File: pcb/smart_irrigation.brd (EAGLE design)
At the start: 76.2 x 76.2 mm, 31 parts, among them IC1 TMP36, IC2 7805DT, IC3 7833DT, IC4 DS1307, J1 1X2-3.5MM, Q1 IRF730, Q2 32.768, Q3 2N3904, U1 BL600

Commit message: PCB: Give names to all signals.
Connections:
- net FLOW_OUT renamed FLOW_DATA
- net N$12 renamed SIO_4
- net N$13 renamed SIO_5
- net N$14 renamed SIO_6
- net N$16 renamed SIO_20
- net N$2 renamed SIO_7
- net N$20 renamed NRESET
- net N$21 renamed SIO_16
- net N$22 renamed SIO_15
- net N$23 renamed SIO_14
- net N$24 renamed SIO_13
- net N$25 renamed SIO_12/SCK
- net N$26 renamed SIO_11/MISO
- net N$27 renamed SIO_10/MOSI
- net N$4 renamed SIO_25
- net N$5 renamed SIO_26
- net N$6 renamed SIO_27
- net N$7 renamed SIO_29
- net RAIN_OUT renamed RAIN_DATA
- net RTC_OUT renamed RTC_DATA
- net SOIL_OUT renamed SOIL_DATA
- net TEMP_OUT renamed TEMP_DATA
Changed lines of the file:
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@@
 <wire x1="32.852" y1="27.178" x2="32.75" y2="27.28" width="0.254" layer="16"/>
 </signal>
-<signal name="N$2">
+<signal name="SIO_7">
 <contactref element="U1" pad="J5_5"/>
 <contactref element="JP4" pad="5"/>
@@
 <wire x1="32.806" y1="21.336" x2="32.75" y2="21.28" width="0.254" layer="16"/>
 </signal>
-<signal name="N$4">
+<signal name="SIO_25">
 <contactref element="JP3" pad="2"/>
 <contactref element="U1" pad="36"/>
@@
 <wire x1="27.362" y1="44.52" x2="26.162" y2="45.72" width="0.254" layer="16"/>
 </signal>
-<signal name="N$5">
+<signal name="SIO_26">
 <contactref element="U1" pad="38"/>
 <contactref element="JP3" pad="3"/>
@@
 <wire x1="26.232" y1="43.25" x2="26.162" y2="43.18" width="0.254" layer="16"/>
 </signal>
-<signal name="N$6">
+<signal name="SIO_27">
 <contactref element="JP3" pad="4"/>
 <contactref element="U1" pad="39"/>
@@
 <wire x1="27.502" y1="41.98" x2="26.162" y2="40.64" width="0.254" layer="16"/>
 </signal>
-<signal name="N$7">
+<signal name="SIO_29">
 <contactref element="U1" pad="41"/>
 <contactref element="JP3" pad="5"/>
@@
 <wire x1="24.638" y1="35.56" x2="26.162" y2="35.56" width="0.254" layer="16"/>
 </signal>
-<signal name="TEMP_OUT">
+<signal name="TEMP_DATA">
 <contactref element="JP3" pad="7"/>
 <contactref element="U1" pad="2"/>
@@
 <wire x1="23.876" y1="33.02" x2="26.162" y2="33.02" width="0.254" layer="16"/>
 </signal>
-<signal name="SOIL_OUT">
+<signal name="SOIL_DATA">
 <contactref element="U1" pad="4"/>
 <contactref element="JP3" pad="8"/>
@@
 <wire x1="6.096" y1="30.48" x2="26.162" y2="30.48" width="0.254" layer="1"/>
 </signal>
-<signal name="RAIN_OUT">
+<signal name="RAIN_DATA">
 <contactref element="JP3" pad="9"/>
 <contactref element="U1" pad="5"/>
@@
 <wire x1="27.208" y1="11.684" x2="27.24" y2="11.652" width="0.254" layer="16"/>
 </signal>
-<signal name="N$12">
+<signal name="SIO_4">
 <contactref element="U1" pad="6"/>
 <contactref element="JP3" pad="10"/>
@@
 <wire x1="27.686" y1="25.4" x2="26.162" y2="25.4" width="0.254" layer="16"/>
 </signal>
-<signal name="N$13">
+<signal name="SIO_5">
 <contactref element="JP3" pad="11"/>
 <contactref element="U1" pad="7"/>
@@
 <wire x1="27.432" y1="22.86" x2="26.162" y2="22.86" width="0.254" layer="16"/>
 </signal>
-<signal name="N$14">
+<signal name="SIO_6">
 <contactref element="U1" pad="8"/>
 <contactref element="JP3" pad="12"/>
@@
 <wire x1="27.178" y1="20.32" x2="26.162" y2="20.32" width="0.254" layer="16"/>
 </signal>
-<signal name="N$16">
+<signal name="SIO_20">
 <contactref element="JP6" pad="2"/>
 <contactref element="U1" pad="27"/>
@@
 <wire x1="57.912" y1="50.546" x2="59.182" y2="50.546" width="0.254" layer="16"/>
 </signal>
-<signal name="RTC_OUT">
+<signal name="RTC_DATA">
 <contactref element="U1" pad="26"/>
 <contactref element="JP6" pad="3"/>
@@
 <wire x1="60.96" y1="48.006" x2="59.182" y2="48.006" width="0.254" layer="16"/>
 </signal>
-<signal name="FLOW_OUT">
+<signal name="FLOW_DATA">
 <contactref element="JP6" pad="4"/>
 <contactref element="U1" pad="25"/>
@@
 <wire x1="59.182" y1="42.926" x2="67.564" y2="42.926" width="0.254" layer="16"/>
 </signal>
-<signal name="N$20">
+<signal name="NRESET">
 <contactref element="JP6" pad="6"/>
 <contactref element="U1" pad="22"/>
@@
 <wire x1="58.276" y1="39.48" x2="59.182" y2="40.386" width="0.254" layer="16"/>
 </signal>
-<signal name="N$21">
+<signal name="SIO_16">
 <contactref element="U1" pad="21"/>
 <contactref element="JP6" pad="7"/>
@@
 <wire x1="58.818" y1="38.21" x2="59.182" y2="37.846" width="0.254" layer="16"/>
 </signal>
-<signal name="N$22">
+<signal name="SIO_15">
 <contactref element="JP6" pad="8"/>
 <contactref element="U1" pad="20"/>
@@
 <wire x1="57.658" y1="35.306" x2="59.182" y2="35.306" width="0.254" layer="16"/>
 </signal>
-<signal name="N$23">
+<signal name="SIO_14">
 <contactref element="U1" pad="19"/>
 <contactref element="JP6" pad="9"/>
@@
 <wire x1="57.658" y1="32.766" x2="59.182" y2="32.766" width="0.254" layer="16"/>
 </signal>
-<signal name="N$24">
+<signal name="SIO_13">
 <contactref element="JP6" pad="10"/>
 <contactref element="U1" pad="18"/>
@@
 <wire x1="58.166" y1="30.226" x2="59.182" y2="30.226" width="0.254" layer="16"/>
 </signal>
-<signal name="N$25">
+<signal name="SIO_12/SCK">
 <contactref element="U1" pad="16"/>
 <contactref element="JP6" pad="11"/>
@@
 <wire x1="53.738" y1="33.13" x2="59.182" y2="27.686" width="0.254" layer="16"/>
 </signal>
-<signal name="N$26">
+<signal name="SIO_11/MISO">
 <contactref element="JP6" pad="12"/>
 <contactref element="U1" pad="15"/>
@@
 <wire x1="57.912" y1="25.146" x2="59.182" y2="25.146" width="0.254" layer="16"/>
 </signal>
-<signal name="N$27">
+<signal name="SIO_10/MOSI">
 <contactref element="U1" pad="14"/>
 <contactref element="JP6" pad="13"/>

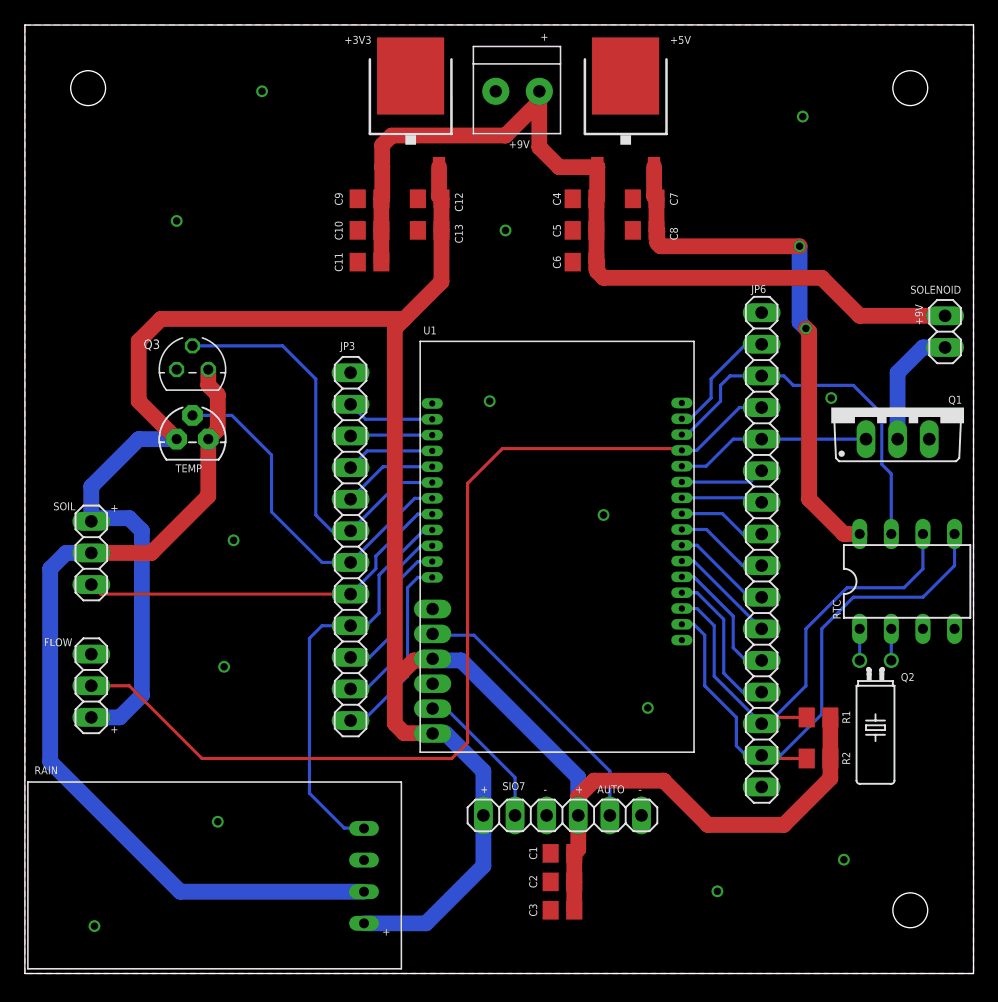
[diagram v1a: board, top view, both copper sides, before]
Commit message: PCB: Fix spacing between headers on BL600 package
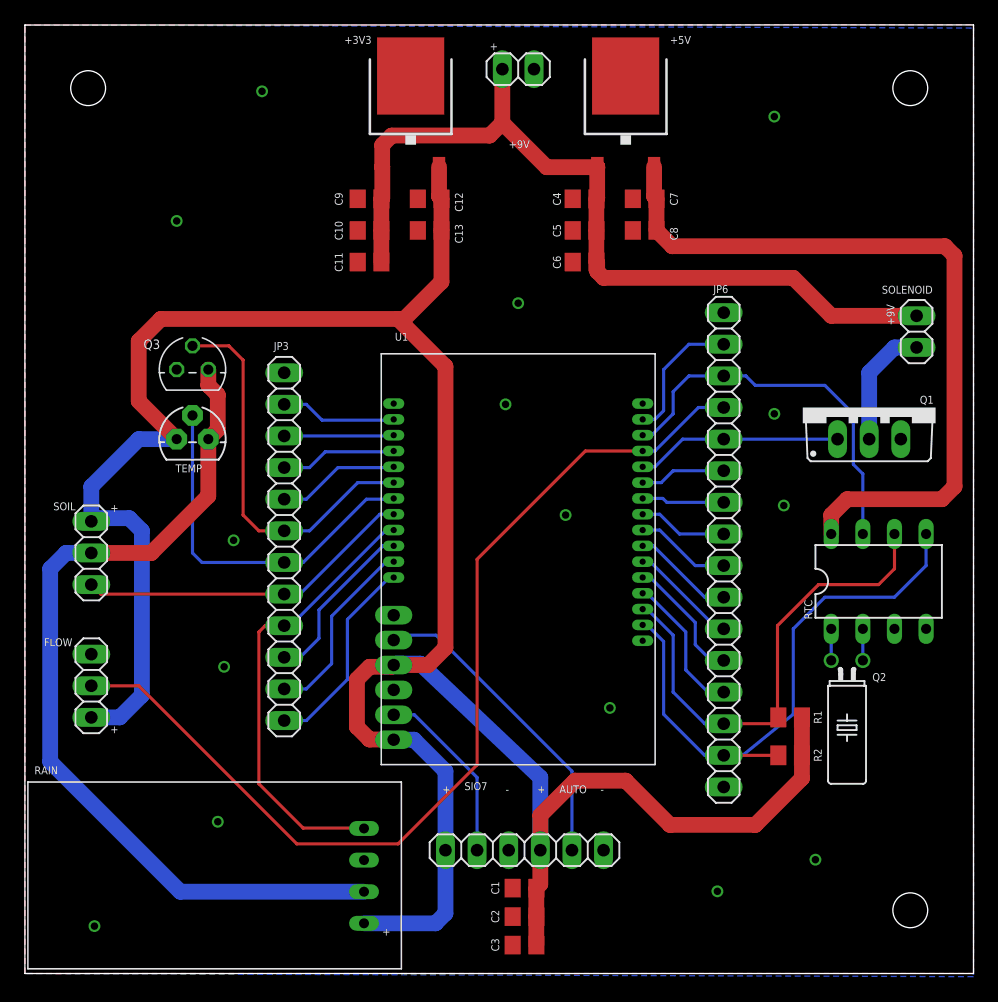
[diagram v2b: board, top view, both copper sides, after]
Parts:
- J1: value 1X2-3.5MM -> (none); device adafruit:1X2-3.5MM -> pinhead:1X02
- moved JP3 5.33 mm to (20.8, 34.3)
- moved C1 4.13 mm to (40.1, 6.86)
- moved C2 4.13 mm to (40.1, 4.57)
- moved C3 4.13 mm to (40.1, 2.29)
- moved JP4 4.13 mm to (40.1, 9.91)
- moved JP6 3.05 mm to (56.1, 34.0)
- moved U1 2.34 mm to (39.6, 33.8)
- moved R2 2.30 mm to (61.5, 17.5)
- moved IC4 2.29 mm to (68.6, 31.5)
- moved JP5 2.29 mm to (71.6, 51.6)
- moved Q1 2.29 mm to (67.8, 45.5)
- moved R1 2.29 mm to (61.5, 20.6)
- moved Q2 2.29 mm to (66.0, 25.1)
- moved J1 1.78 mm to (39.6, 72.6)
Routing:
- net +5V: track 43.6 -> 60.9 mm, vias 2 -> 0
- net +3V3: track 199.6 -> 207.4 mm
- net SOIL_DATA: track 31.0 -> 27.3 mm
- net +9V: track 72.1 -> 68.9 mm
- net RAIN_DATA: track 33.2 -> 36.3 mm
- net NAUTORUN: track 22.4 -> 25.4 mm
- net SIO_7: track 12.0 -> 14.6 mm
- net SIO_25: track 7.06 -> 9.35 mm
- net SIO_27: track 7.11 -> 9.35 mm
- net SIO_26: track 6.59 -> 8.82 mm
- net SIO_29: track 7.64 -> 9.87 mm
- net SENSORS_ENABLE: track 33.4 -> 31.2 mm
- net RTC_DATA: track 30.0 -> 31.2 mm
- net SIO_20: track 9.78 -> 10.9 mm
- net SDA: track 46.6 -> 47.6 mm
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
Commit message: PCB: Change flow sensor GPIO pin
The flow sensor's pin was on the opposite side of the other sensors,
making for awkward routing.
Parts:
- moved JP7 23.9 mm to (5.33, 47.0)
- moved IC1 0.25 mm to (13.5, 42.7)
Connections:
- removed net SIO_29: JP3.5, U1.41
- new net SIO_18: JP6.4, U1.25
- net FLOW_DATA: now also JP3.5, U1.41; no longer JP6.4, U1.25
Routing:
- net FLOW_DATA: track 80.3 -> 32.3 mm
- net +3V3: track 207.4 -> 186.4 mm
- net SIO_29: track 9.87 -> 0.00 mm
- net SIO_18: track 0.00 -> 7.96 mm
- net TEMP_DATA: track 29.7 -> 27.2 mm
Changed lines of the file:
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@@
 <text x="4.064" y="37.846" size="0.635" layer="25" font="vector" ratio="20" rot="R180">SOIL</text>
 <text x="6.858" y="37.084" size="0.635" layer="25" font="vector" ratio="20">+</text>
-<text x="3.81" y="26.924" size="0.635" layer="25" font="vector" ratio="20" rot="R180">FLOW</text>
+<text x="4.572" y="51.562" size="0.635" layer="25" font="vector" ratio="20" rot="R180">FLOW</text>
 <text x="6.858" y="19.304" size="0.635" layer="25" font="vector" ratio="20">+</text>
 <text x="0.762" y="16.002" size="0.635" layer="25" font="vector" ratio="20">RAIN</text>
@@
 <attribute name="NAME" x="64.008" y="20.066" size="0.635" layer="25" font="vector" ratio="20" rot="R90"/>
 </element>
-<element name="IC1" library="smart_irrigation" package="TO92" value="TMP36" x="13.462" y="42.926" smashed="yes"/>
+<element name="IC1" library="smart_irrigation" package="TO92" value="TMP36" x="13.462" y="42.672" smashed="yes"/>
 <element name="JP2" library="pinhead" package="1X03" value="" x="5.334" y="33.782" smashed="yes" rot="R270">
 <attribute name="VALUE" x="2.159" y="37.592" size="1.27" layer="27" rot="R270"/>
@@
 <attribute name="NAME" x="38.1" y="1.778" size="0.635" layer="25" font="vector" ratio="20" rot="R90"/>
 </element>
-<element name="JP7" library="smart_irrigation" package="1X03" value="" x="5.334" y="23.114" smashed="yes" rot="R90">
-<attribute name="VALUE" x="8.509" y="19.304" size="1.27" layer="27" rot="R90"/>
+<element name="JP7" library="smart_irrigation" package="1X03" value="" x="5.334" y="46.99" smashed="yes" rot="R90">
+<attribute name="VALUE" x="8.509" y="43.18" size="1.27" layer="27" rot="R90"/>
 </element>
 <element name="Q1" library="smart_irrigation" package="TO220" value="IRF730" x="67.818" y="45.466" smashed="yes">
@@
 <wire x1="31.75" y1="24.892" x2="29.836" y2="24.892" width="1.27" layer="16"/>
 <wire x1="29.836" y1="24.892" x2="29.624" y2="24.782" width="1.27" layer="16"/>
-<wire x1="5.334" y1="20.574" x2="7.62" y2="20.574" width="1.27" layer="16"/>
-<wire x1="7.62" y1="20.574" x2="9.398" y2="22.352" width="1.27" layer="16"/>
-<wire x1="9.398" y1="22.352" x2="9.398" y2="35.56" width="1.27" layer="16"/>
-<wire x1="9.398" y1="35.56" x2="8.382" y2="36.576" width="1.27" layer="16"/>
-<wire x1="8.382" y1="36.576" x2="5.588" y2="36.576" width="1.27" layer="16"/>
-<wire x1="5.588" y1="36.576" x2="5.334" y2="36.322" width="1.27" layer="16"/>
-<wire x1="12.192" y1="42.926" x2="9.144" y2="42.926" width="1.27" layer="16"/>
-<wire x1="9.144" y1="42.926" x2="5.334" y2="39.116" width="1.27" layer="16"/>
-<wire x1="5.334" y1="39.116" x2="5.334" y2="36.322" width="1.27" layer="16"/>
 <wire x1="33.462" y1="59.69" x2="33.462" y2="55.56" width="1.27" layer="1"/>
 <wire x1="33.462" y1="55.56" x2="30.48" y2="52.578" width="1.27" layer="1"/>
@@
 <wire x1="29.972" y1="52.578" x2="10.922" y2="52.578" width="1.27" layer="1"/>
 <wire x1="10.922" y1="52.578" x2="9.144" y2="50.8" width="1.27" layer="1"/>
-<wire x1="9.144" y1="50.8" x2="9.144" y2="45.974" width="1.27" layer="1"/>
-<wire x1="9.144" y1="45.974" x2="12.192" y2="42.926" width="1.27" layer="1"/>
+<wire x1="9.144" y1="50.8" x2="9.144" y2="45.72" width="1.27" layer="1"/>
+<wire x1="9.144" y1="45.72" x2="12.192" y2="42.672" width="1.27" layer="1"/>
 <contactref element="C3" pad="1"/>
 <wire x1="41.082" y1="4.572" x2="41.082" y2="2.286" width="1.27" layer="1"/>
@@
 <wire x1="33.782" y1="16.256" x2="31.256" y2="18.782" width="1.27" layer="16"/>
 <wire x1="31.256" y1="18.782" x2="29.624" y2="18.782" width="1.27" layer="16"/>
+<wire x1="5.334" y1="36.322" x2="5.334" y2="44.45" width="1.27" layer="1"/>
+<wire x1="5.334" y1="44.45" x2="8.128" y2="44.45" width="1.27" layer="1"/>
+<wire x1="8.128" y1="44.45" x2="9.144" y2="45.72" width="1.27" layer="1"/>
 </signal>
 <signal name="NAUTORUN">
@@
 <wire x1="29.562" y1="41.91" x2="29.624" y2="41.972" width="0.254" layer="16"/>
 </signal>
-<signal name="SIO_29">
+<signal name="FLOW_DATA">
 <contactref element="U1" pad="41"/>
 <contactref element="JP3" pad="5"/>
@@
 <wire x1="25.146" y1="40.64" x2="29.562" y2="40.64" width="0.254" layer="16"/>
 <wire x1="29.562" y1="40.64" x2="29.624" y2="40.702" width="0.254" layer="16"/>
+<contactref element="JP7" pad="2"/>
+<wire x1="5.334" y1="46.99" x2="7.874" y2="46.99" width="0.254" layer="16"/>
+<wire x1="7.874" y1="46.99" x2="8.89" y2="46.228" width="0.254" layer="16"/>
+<wire x1="8.89" y1="46.228" x2="16.764" y2="46.228" width="0.254" layer="16"/>
+<wire x1="16.764" y1="46.228" x2="18.542" y2="44.45" width="0.254" layer="16"/>
+<wire x1="18.542" y1="44.45" x2="18.542" y2="38.862" width="0.254" layer="16"/>
+<wire x1="18.542" y1="38.862" x2="19.304" y2="38.1" width="0.254" layer="16"/>
+<wire x1="19.304" y1="38.1" x2="20.828" y2="38.1" width="0.254" layer="16"/>
 </signal>
 <signal name="SENSORS_ENABLE">
@@
 <contactref element="U1" pad="2"/>
 <contactref element="IC1" pad="2"/>
-<wire x1="13.462" y1="44.831" x2="13.462" y2="33.782" width="0.254" layer="16"/>
-<wire x1="13.462" y1="33.782" x2="14.224" y2="33.02" width="0.254" layer="16"/>
-<wire x1="14.224" y1="33.02" x2="20.828" y2="33.02" width="0.254" layer="16"/>
 <wire x1="20.828" y1="33.02" x2="22.352" y2="33.02" width="0.254" layer="16"/>
 <wire x1="22.352" y1="33.02" x2="27.432" y2="38.1" width="0.254" layer="16"/>
 <wire x1="27.432" y1="38.1" x2="29.562" y2="38.1" width="0.254" layer="16"/>
 <wire x1="29.562" y1="38.1" x2="29.624" y2="38.162" width="0.254" layer="16"/>
+<wire x1="20.828" y1="33.02" x2="20.066" y2="33.02" width="0.254" layer="16"/>
+<wire x1="20.066" y1="33.02" x2="16.51" y2="36.576" width="0.254" layer="16"/>
+<wire x1="16.51" y1="36.576" x2="16.51" y2="43.434" width="0.254" layer="16"/>
+<wire x1="16.51" y1="43.434" x2="15.24" y2="44.704" width="0.254" layer="16"/>
+<wire x1="15.24" y1="44.704" x2="13.589" y2="44.704" width="0.254" layer="16"/>
+<wire x1="13.589" y1="44.704" x2="13.462" y2="44.577" width="0.254" layer="16"/>
 </signal>
 <signal name="SOIL_DATA">
@@
 <wire x1="52.07" y1="46.736" x2="53.34" y2="48.006" width="0.254" layer="16"/>
 <wire x1="53.34" y1="48.006" x2="56.134" y2="48.006" width="0.254" layer="16"/>
-</signal>
-<signal name="FLOW_DATA">
-<contactref element="JP6" pad="4"/>
-<contactref element="U1" pad="25"/>
-<contactref element="JP7" pad="2"/>
-<wire x1="49.624" y1="41.972" x2="45.02" y2="41.972" width="0.254" layer="1"/>
-<wire x1="45.02" y1="41.972" x2="36.322" y2="33.274" width="0.254" layer="1"/>
-<wire x1="36.322" y1="33.274" x2="36.322" y2="16.764" width="0.254" layer="1"/>
-<wire x1="36.322" y1="16.764" x2="29.972" y2="10.414" width="0.254" layer="1"/>
-<wire x1="29.972" y1="10.414" x2="21.844" y2="10.414" width="0.254" layer="1"/>
-<wire x1="21.844" y1="10.414" x2="9.144" y2="23.114" width="0.254" layer="1"/>
-<wire x1="9.144" y1="23.114" x2="5.334" y2="23.114" width="0.254" layer="1"/>
-<wire x1="49.624" y1="41.972" x2="50.608" y2="41.972" width="0.254" layer="16"/>
-<wire x1="50.608" y1="41.972" x2="54.102" y2="45.466" width="0.254" layer="16"/>
-<wire x1="54.102" y1="45.466" x2="56.134" y2="45.466" width="0.254" layer="16"/>
 </signal>
 <signal name="SOL_ENABLE">
@@
 <wire x1="5.334" y1="33.782" x2="10.16" y2="33.782" width="1.27" layer="1"/>
 <wire x1="10.16" y1="33.782" x2="14.732" y2="38.354" width="1.27" layer="1"/>
-<wire x1="14.732" y1="38.354" x2="14.732" y2="42.926" width="1.27" layer="1"/>
+<wire x1="14.732" y1="38.354" x2="14.732" y2="42.672" width="1.27" layer="1"/>
 <wire x1="14.732" y1="48.514" x2="14.732" y2="47.244" width="1.27" layer="1"/>
-<wire x1="14.732" y1="47.244" x2="15.494" y2="46.482" width="1.27" layer="1"/>
-<wire x1="15.494" y1="46.482" x2="15.494" y2="43.688" width="1.27" layer="1"/>
-<wire x1="15.494" y1="43.688" x2="14.732" y2="42.926" width="1.27" layer="1"/>
+<wire x1="14.732" y1="47.244" x2="15.748" y2="46.228" width="1.27" layer="1"/>
+<wire x1="15.748" y1="46.228" x2="15.748" y2="43.942" width="1.27" layer="1"/>
+<wire x1="15.748" y1="43.942" x2="14.732" y2="42.672" width="1.27" layer="1"/>
 </signal>
 <signal name="N$1">
@@
 <wire x1="67.31" y1="27.686" x2="67.31" y2="25.146" width="0.254" layer="16"/>
 </signal>
+<signal name="SIO_18">
+<contactref element="JP6" pad="4"/>
+<contactref element="U1" pad="25"/>
+<wire x1="49.624" y1="41.972" x2="50.608" y2="41.972" width="0.254" layer="16"/>
+<wire x1="50.608" y1="41.972" x2="54.102" y2="45.466" width="0.254" layer="16"/>
+<wire x1="54.102" y1="45.466" x2="56.134" y2="45.466" width="0.254" layer="16"/>
+</signal>
 </signals>

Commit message: PCB: Move terminal block farther into board
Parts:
- moved J1 2.03 mm to (39.6, 70.6)
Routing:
- net +9V: track 68.9 -> 66.9 mm
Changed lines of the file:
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@@
 <text x="25.654" y="74.676" size="0.635" layer="25" font="vector" ratio="20">+3V3</text>
 <text x="51.816" y="74.676" size="0.635" layer="25" font="vector" ratio="20">+5V</text>
-<text x="37.338" y="74.168" size="0.635" layer="25" font="vector" ratio="20">+</text>
+<text x="37.084" y="71.882" size="0.635" layer="25" font="vector" ratio="20">+</text>
 <text x="14.224" y="40.894" size="0.635" layer="25" font="vector" ratio="20" rot="R180">TEMP</text>
 </plain>
@@
 <elements>
 <element name="IC2" library="linear" package="TO252" value="7805DT" x="48.26" y="69.596" smashed="yes"/>
-<element name="J1" library="pinhead" package="1X02" value="" x="39.624" y="72.644" smashed="yes" rot="R180"/>
+<element name="J1" library="pinhead" package="1X02" value="" x="39.624" y="70.612" smashed="yes" rot="R180"/>
 <element name="C8" library="rcl" package="C0805" value="10uF" x="49.784" y="59.69" smashed="yes" rot="R180">
 <attribute name="NAME" x="51.816" y="59.944" size="0.635" layer="25" font="vector" ratio="20" rot="R270"/>
@@
 <wire x1="45.974" y1="56.388" x2="45.974" y2="57.084" width="1.27" layer="1"/>
 <wire x1="45.974" y1="57.084" x2="45.908" y2="57.15" width="1.27" layer="1"/>
-<wire x1="38.354" y1="72.644" x2="38.354" y2="68.326" width="1.27" layer="1"/>
+<wire x1="38.354" y1="70.612" x2="38.354" y2="68.326" width="1.27" layer="1"/>
 <wire x1="38.354" y1="68.326" x2="37.338" y2="67.31" width="1.27" layer="1"/>
 <wire x1="37.338" y1="67.31" x2="29.464" y2="67.31" width="1.27" layer="1"/>
